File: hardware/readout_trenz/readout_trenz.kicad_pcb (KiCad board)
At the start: 6 copper layers, 377 parts, among them J1 Conn_Coaxial, J10 SparkfunFT232RL, J11 TrenzSFP+cage, J12 Trenz_Module, J13 Conn_02x05_Odd_Even, J14 BNC, J15 ERM8-060-05.0-L-DV, J16 ERM8-060-05.0-L-DV, J17 ERM8-060-05.0-L-DV, J18 ERM8-060-05.0-L-DV, J19 ERM8-060-05.0-L-DV, J2 Conn_Coaxial, J3 Conn_Coaxial_Power, J4 Conn_02x05_Odd_Even, J5 Conn_01x10, J7 BNC, J8 ERM8-060-05.0-L-DV, J9 Digilent JTAG header, Q1 DMN67D7L, Q2 DMN67D7L, Q3 DMN67D7L, Q4 DMN67D7L, Q5 DMN67D7L, Q6 DMN67D7L, U1 SN74AXC2T45DCTR, U10 NLSV8T244, U11 DS90LV027A, U12 ADS7955, U13 REF5025, U14 SN74AXC2T45DCTR, U15 CITIROC1A, U16 SN74AXC2T45DCTR, U17 NLSV8T244, U18 NLSV8T244, U19 DS90LV027A, U2 LP2985-5.0, U20 ADS7955, U21 REF5025, U22 SN74AXC2T45DCTR, U3 NCP718xSN180, U4 LT1963AxQ-3.3, U5 LT1963AxQ-3.3, U6 LT1963AxQ-3.3, U7 CITIROC1A, U8 SN74AXC2T45DCTR, U9 NLSV8T244

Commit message: -
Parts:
- removed the U15 at (348.6, 175.0)
- moved C89 3.39 mm to (397.6, 136.3), turned to 0 degrees
- moved C171 3.39 mm to (339.0, 136.9), turned to 0 degrees
- moved C70 3.39 mm to (412.1, 161.2), turned to 270 degrees
- moved C88 3.39 mm to (397.6, 139.7), turned to 0 degrees
- moved C74 3.38 mm to (415.5, 161.2), turned to 90 degrees
- moved C172 3.38 mm to (339.0, 133.5), turned to 0 degrees
- moved C77 2.61 mm to (416.4, 168.0)
- moved C80 2.26 mm to (418.0, 122.3)
- moved C163 2.26 mm to (317.5, 132.6)
- moved C69 2.23 mm to (408.6, 122.3)
- moved C68 2.17 mm to (408.6, 138.9)
- moved C79 2.15 mm to (417.9, 138.9)
- moved C152 2.10 mm to (326.9, 132.6)
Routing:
- net 3.3V_CITIROC: track 88.0 -> 65.3 mm, vias 40 -> 30
- net GNDD: track 37.0 -> 28.0 mm, vias 37 -> 28
- net GNDA: track 96.0 -> 89.0 mm, vias 55 -> 48
- net 1.8V_CITIROC: track 15.5 -> 10.4 mm, vias 12 -> 8
- net Net-(C154-Pad2): track 9.10 -> 4.55 mm, vias 2 -> 1
- net Net-(C150-Pad2): track 8.25 -> 4.12 mm, vias 4 -> 2
- net Net-(TP16-Pad1): track 7.65 -> 3.82 mm
- net Net-(R111-Pad2): track 6.52 -> 2.84 mm, vias 2 -> 1
- net /CITIROC_1/Fast_Trig1: track 5.87 -> 2.94 mm, vias 2 -> 1
- net Net-(C148-Pad2): track 5.57 -> 2.79 mm, vias 2 -> 1
- net Net-(TP15-Pad1): track 5.41 -> 2.71 mm
- net Net-(C149-Pad2): track 5.41 -> 2.71 mm, vias 2 -> 1
- net Net-(R112-Pad2): track 4.92 -> 2.46 mm, vias 2 -> 1
- net Net-(R112-Pad1): track 4.87 -> 2.46 mm, vias 2 -> 1
- net Net-(R111-Pad1): track 4.96 -> 2.73 mm, vias 2 -> 1
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
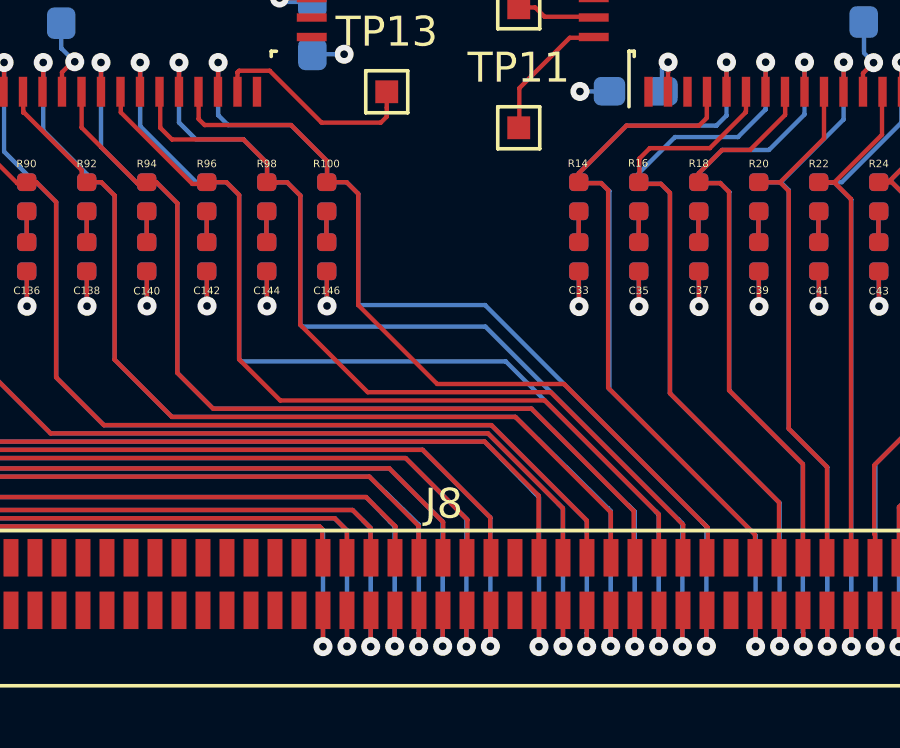
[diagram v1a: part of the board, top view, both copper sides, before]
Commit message: Readout Prototype Layout in progress
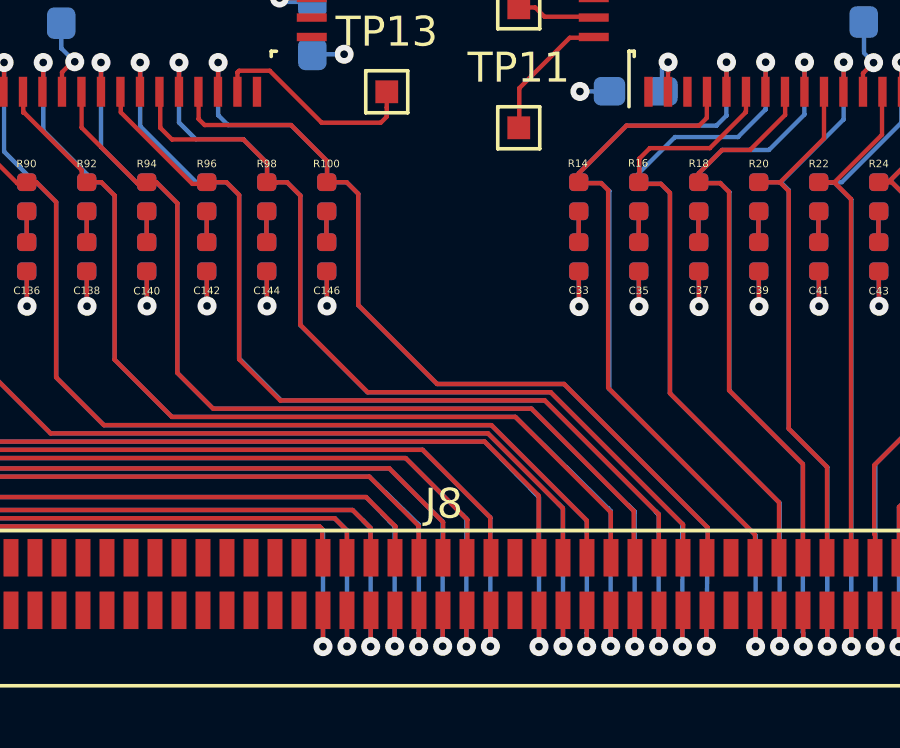
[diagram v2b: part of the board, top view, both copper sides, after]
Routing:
- net /CITIROC_1/SIPM_IN29: track 33.8 -> 34.7 mm

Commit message: Layout in progress
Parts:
- added J6: Conn_01x10, Connector_PinHeader_2.54mm:PinHeader_2x05_P2.54mm_Vertical, F.Cu at (214.2, 144.8)
- C96: moved to B.Cu
- J4: footprint Connector_PinHeader_2.54mm:PinHeader_2x05_P2.54mm_Vertical -> Connector_PinHeader_2.54mm:PinHeader_2x04_P2.54mm_Vertical
- U10, U17, U18, U9: footprint Package_SO:SOIC-20W_7.5x12.8mm_P1.27mm -> Package_SO:TSSOP-20_4.4x6.5mm_P0.65mm
- moved U10 57.5 mm to (356.7, 116.2), turned to 270 degrees
- moved U9 56.4 mm to (363.9, 116.2), turned to 270 degrees
- moved C162 51.1 mm to (366.8, 135.4), turned to 180 degrees
- moved C151 44.6 mm to (366.8, 129.5), turned to 180 degrees
- moved U17 44.4 mm to (365.0, 132.4), turned to 270 degrees
- moved C163 42.2 mm to (359.6, 135.3), turned to 180 degrees
- moved R105 39.5 mm to (310.0, 142.5), turned to 0 degrees
- moved R51 38.6 mm to (426.0, 157.5), turned to 0 degrees
- moved R106 36.4 mm to (310.0, 145.0), turned to 0 degrees
- moved R52 36.0 mm to (426.0, 155.0), turned to 0 degrees
- moved U18 35.9 mm to (357.9, 132.4), turned to 270 degrees
- moved R46 33.6 mm to (426.0, 152.5), turned to 0 degrees
- moved R104 33.4 mm to (310.0, 147.5), turned to 0 degrees
- moved C152 32.9 mm to (359.6, 129.5), turned to 180 degrees
- moved R47 31.4 mm to (426.0, 150.0), turned to 0 degrees
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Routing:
- net /CITIROC_1/TRIG_OUT26: track 0.00 -> 22.9 mm, vias 0 -> 2
- net /CITIROC_1/TRIG_OUT30: track 0.00 -> 21.5 mm, vias 0 -> 2
- net /CITIROC_1/TRIG_OUT28: track 0.00 -> 21.3 mm, vias 0 -> 2
- net /CITIROC_1/TRIG_OUT29: track 0.00 -> 19.8 mm, vias 0 -> 2
- net /CITIROC_1/TRIG_OUT25: track 0.00 -> 19.1 mm, vias 0 -> 2
- net /CITIROC_1/TRIG_OUT27: track 0.00 -> 17.1 mm
- net /CITIROC_1/TRIG_OUT31: track 0.00 -> 16.9 mm
- net GNDA: track 89.0 -> 103.3 mm, vias 48 -> 54
- net GNDD: track 28.0 -> 41.3 mm
- net 3.3V_CITIROC: track 65.3 -> 68.5 mm
- net 1.8V_CITIROC: track 10.4 -> 13.5 mm
- net /CITIROC_1/SIPM_IN30: track 27.0 -> 25.0 mm, vias 0 -> 2
- net /CITIROC_1/SIPM_IN31: track 32.5 -> 30.6 mm, vias 2 -> 3
- net /CITIROC_1/SIPM_IN19: track 38.9 -> 37.1 mm, vias 2 -> 3
- net /CITIROC_1/SIPM_IN3: track 52.2 -> 50.7 mm, vias 2 -> 3
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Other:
- net class Power added: clearance 0.127, trace_width 0.254, via_dia 0.635, via_drill 0.254

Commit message: Layout in progress
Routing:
- net /CITIROC_1/TRIG_OUT5: track 0.00 -> 39.9 mm, vias 0 -> 2
- net /CITIROC_1/TRIG_OUT9: track 0.00 -> 39.9 mm, vias 0 -> 2
- net /CITIROC_1/TRIG_OUT13: track 0.00 -> 39.8 mm, vias 0 -> 2
- net /CITIROC_1/TRIG_OUT12: track 0.00 -> 39.5 mm, vias 0 -> 2
- net /CITIROC_1/TRIG_OUT8: track 0.00 -> 39.5 mm, vias 0 -> 2
- net /CITIROC_1/TRIG_OUT4: track 0.00 -> 39.1 mm, vias 0 -> 2
- net /CITIROC_1/TRIG_OUT1: track 0.00 -> 36.8 mm, vias 0 -> 2
- net /CITIROC_1/TRIG_OUT0: track 0.00 -> 35.7 mm, vias 0 -> 2
- net /CITIROC_1/TRIG_OUT10: track 0.00 -> 33.7 mm, vias 0 -> 2
- net /CITIROC_1/TRIG_OUT11: track 0.00 -> 33.5 mm, vias 0 -> 2
- net /CITIROC_1/TRIG_OUT6: track 0.00 -> 33.4 mm, vias 0 -> 2
- net /CITIROC_1/TRIG_OUT7: track 0.00 -> 33.4 mm, vias 0 -> 2
- net /CITIROC_1/TRIG_OUT2: track 0.00 -> 33.1 mm, vias 0 -> 2
- net /CITIROC_1/TRIG_OUT3: track 0.00 -> 33.0 mm, vias 0 -> 2
- net /CITIROC_1/TRIG_OUT14: track 0.00 -> 32.8 mm, vias 0 -> 2
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
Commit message: Layout in progress
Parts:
- R102, R103, R104, R105, R106, R107, R108, R46, R47, R48, R49, R50, R51, R52, U14, U16, U19, U22: moved to B.Cu
- moved R103 59.4 mm to (359.6, 182.7)
- moved R104 59.1 mm to (359.6, 179.7)
- moved R102 58.9 mm to (359.6, 184.2)
- moved R105 58.5 mm to (359.6, 173.6)
- moved R108 58.3 mm to (359.6, 185.7)
- moved R106 58.0 mm to (359.6, 175.1)
- moved R107 57.8 mm to (359.6, 187.2)
- moved C80 44.1 mm to (374.9, 131.8), turned to 180 degrees
- moved R47 43.0 mm to (398.0, 182.6)
- moved R48 42.6 mm to (398.0, 179.6)
- moved R46 42.2 mm to (398.0, 184.1)
- moved R49 41.8 mm to (398.0, 173.6)
- moved R52 41.5 mm to (398.0, 185.6)
- moved R50 41.1 mm to (398.0, 175.1)
- moved R51 40.7 mm to (398.0, 187.1)
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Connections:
- J12 pad A31: /CITIROC_1/ADC_SERIAL0 -> /CITIROC_2/Serial_ctrl0
- J12 pad A32: /CITIROC_2/ADC_SERIAL0 -> /CITIROC_2/SH_Ctrl0
- J12 pad A33: /CITIROC_1/ADC_SERIAL1 -> /CITIROC_2/Serial_ctrl1
- J12 pad A34: /CITIROC_2/ADC_SERIAL1 -> /CITIROC_2/SH_Ctrl1
- J12 pad A35: /CITIROC_1/ADC_SERIAL2 -> /CITIROC_2/Serial_ctrl2
- J12 pad A36: /CITIROC_2/ADC_SERIAL2 -> /CITIROC_2/SH_Ctrl2
- J12 pad A37: /CITIROC_1/ADC_SERIAL3 -> /CITIROC_2/Serial_ctrl3
- J12 pad A38: /CITIROC_2/ADC_SERIAL3 -> /CITIROC_2/SH_Ctrl3
- J12 pad A39: /CITIROC_1/SH_Ctrl0 -> /CITIROC_2/Serial_ctrl4
- J12 pad A40: /CITIROC_2/SH_Ctrl0 -> /CITIROC_2/SH_Ctrl4
- J12 pad A41: /CITIROC_1/SH_Ctrl1 -> /CITIROC_2/Serial_ctrl5
- J12 pad A42: /CITIROC_2/SH_Ctrl1 -> /CITIROC_2/SH_Ctrl5
- J12 pad A43: /CITIROC_1/SH_Ctrl2 -> /CITIROC_2/Serial_ctrl6
- J12 pad A44: /CITIROC_2/SH_Ctrl2 -> /CITIROC_2/SH_Ctrl6
- J12 pad A45: /CITIROC_1/SH_Ctrl3 -> /CITIROC_2/Serial_ctrl7
- J12 pad A46: /CITIROC_2/SH_Ctrl3 -> /CITIROC_2/SH_Ctrl7
- J12 pad A49: /CITIROC_1/SH_Ctrl4 -> /CITIROC_2/Serial_ctrl8
- J12 pad A50: /CITIROC_2/SH_Ctrl4 -> /CITIROC_2/SH_Ctrl8
- J12 pad A51: /CITIROC_1/SH_Ctrl5 -> /CITIROC_1/SH_Ctrl0
- J12 pad A52: /CITIROC_2/SH_Ctrl5 -> /CITIROC_2/SH_Ctrl9
- J12 pad A53: /CITIROC_1/SH_Ctrl6 -> /CITIROC_1/SH_Ctrl1
- J12 pad A54: /CITIROC_2/SH_Ctrl6 -> /CITIROC_1/ADC_SERIAL0
- J12 pad A55: /CITIROC_1/SH_Ctrl7 -> /CITIROC_1/SH_Ctrl2
- J12 pad A56: /CITIROC_2/SH_Ctrl7 -> /CITIROC_1/ADC_SERIAL1
- J12 pad A57: /CITIROC_1/SH_Ctrl8 -> /CITIROC_1/SH_Ctrl3
- J12 pad A58: /CITIROC_2/SH_Ctrl8 -> /CITIROC_1/ADC_SERIAL2
- J12 pad A59: /CITIROC_1/SH_Ctrl9 -> /CITIROC_1/SH_Ctrl4
- J12 pad A60: /CITIROC_2/SH_Ctrl9 -> /CITIROC_1/ADC_SERIAL3
- J12 pad A62: /Trenz_Module/TEST0 -> /CITIROC_2/ADC_SERIAL0
- J12 pad A63: /Trenz_Module/TEST1 -> /CITIROC_1/SH_Ctrl5
- J12 pad A64: /CITIROC_2/Serial_ctrl0 -> /CITIROC_2/ADC_SERIAL1
- J12 pad A65: /CITIROC_1/Serial_ctrl0 -> /CITIROC_1/SH_Ctrl6
- J12 pad A67: /CITIROC_1/Serial_ctrl1 -> /CITIROC_1/SH_Ctrl7
- J12 pad A68: /CITIROC_2/Serial_ctrl1 -> /CITIROC_2/ADC_SERIAL2
- J12 pad A69: /CITIROC_1/Serial_ctrl2 -> /CITIROC_1/SH_Ctrl8
- J12 pad A70: /CITIROC_2/Serial_ctrl2 -> /CITIROC_2/ADC_SERIAL3
- J12 pad A71: /CITIROC_1/Serial_ctrl3 -> /CITIROC_1/SH_Ctrl9
- J12 pad A72: /CITIROC_2/Serial_ctrl3 -> /CITIROC_1/Fast_Trig0
- J12 pad A73: /CITIROC_1/Serial_ctrl4 -> /CITIROC_1/Serial_ctrl0
- J12 pad A74: /CITIROC_2/Serial_ctrl4 -> /CITIROC_1/Fast_Trig1
- J12 pad A75: /CITIROC_1/Serial_ctrl5 -> /CITIROC_1/Serial_ctrl1
- J12 pad A76: /CITIROC_2/Serial_ctrl5 -> /CITIROC_1/Fast_Trig2
- J12 pad A77: /CITIROC_1/Serial_ctrl6 -> /CITIROC_1/Serial_ctrl2
- J12 pad A78: /CITIROC_2/Serial_ctrl6 -> /CITIROC_1/Fast_Trig3
- J12 pad A79: /CITIROC_1/Serial_ctrl7 -> /CITIROC_1/Serial_ctrl3
- J12 pad A80: /CITIROC_2/Serial_ctrl7 -> /Trenz_Module/TEST0
- J12 pad A81: /CITIROC_1/Serial_ctrl8 -> /CITIROC_1/Serial_ctrl4
- J12 pad A82: /CITIROC_2/Serial_ctrl8 -> /Trenz_Module/TEST1
- J12 pad A85: /POWER/ENABLE -> /CITIROC_1/Serial_ctrl5
- J12 pad A87: /Trenz_Module/TEST2 -> /CITIROC_1/Serial_ctrl6
- J12 pad A89: /CITIROC_1/Fast_Trig0 -> /CITIROC_1/Serial_ctrl7
- J12 pad A91: /CITIROC_1/Fast_Trig1 -> /CITIROC_1/Serial_ctrl8
- J12 pad A93: /CITIROC_1/Fast_Trig2 -> /Trenz_Module/TEST2
- J12 pad A95: /CITIROC_1/Fast_Trig3 -> /POWER/ENABLE
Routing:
- net /CITIROC_2/Serial_ctrl3: track 0.00 -> 10.2 mm
- net /CITIROC_2/Serial_ctrl2: track 0.00 -> 10.1 mm
- net /CITIROC_2/Serial_ctrl0: track 0.00 -> 10.1 mm
- net /CITIROC_2/Serial_ctrl1: track 0.00 -> 10.0 mm
- net /CITIROC_2/Serial_ctrl4: track 0.00 -> 9.79 mm
- net /CITIROC_2/Serial_ctrl5: track 0.00 -> 9.47 mm
- net /CITIROC_2/Serial_ctrl6: track 0.00 -> 9.14 mm
- net /CITIROC_1/Serial_ctrl4: track 0.00 -> 7.97 mm
- net /CITIROC_1/Serial_ctrl3: track 0.00 -> 7.94 mm
- net /CITIROC_1/Serial_ctrl6: track 0.00 -> 7.89 mm
- net /CITIROC_1/Serial_ctrl2: track 0.00 -> 7.87 mm
- net /CITIROC_1/Serial_ctrl1: track 0.00 -> 7.76 mm
- net /CITIROC_1/Serial_ctrl5: track 0.00 -> 7.75 mm
- net /CITIROC_1/Serial_ctrl0: track 0.00 -> 7.72 mm
- net /CITIROC_1/SH_Ctrl5: track 0.00 -> 6.99 mm
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
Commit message: Layout ion progress
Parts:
- added C12: 1uF, Capacitor_SMD:C_0603_1608Metric_Pad1.05x0.95mm_HandSolder, F.Cu at (253.3, 132.2)
- added C7: 1uF, Capacitor_SMD:C_0603_1608Metric_Pad1.05x0.95mm_HandSolder, F.Cu at (244.8, 131.3)
- added D9: Red_LED, LED_THT:LED_D3.0mm, F.Cu at (230.0, 102.4)
- added Q3: DMN67D7L, Package_TO_SOT_SMD:SOT-23, F.Cu at (232.2, 107.2)
- added R14: 80, Resistor_SMD:R_0603_1608Metric_Pad1.05x0.95mm_HandSolder, F.Cu at (229.6, 106.3)
- added U4: NCP718xSN180, Package_TO_SOT_SMD:TSOT-23-5_HandSoldering, F.Cu at (249.5, 132.3)
- C162: renamed from C160; moved to F.Cu
- C79: renamed from C77; moved to F.Cu
- U12: renamed from U11; moved to B.Cu
- U9: renamed from U8; moved to B.Cu
- moved U17 52.1 mm to (363.0, 135.0)
- moved U20 50.8 mm to (367.8, 159.8), turned to 270 degrees
- moved C162 50.5 mm to (366.8, 157.3), turned to 180 degrees
- moved C159 50.2 mm to (359.5, 136.3), turned to 0 degrees
- moved C155 48.5 mm to (359.5, 133.7), turned to 180 degrees
- moved C76 43.8 mm to (379.5, 136.3), turned to 0 degrees
- moved C72 42.6 mm to (379.5, 133.7), turned to 180 degrees
- moved U9 40.4 mm to (383.0, 135.0), turned to 270 degrees
- moved C88 39.9 mm to (374.5, 69.2)
- moved U21 39.9 mm to (365.3, 69.0)
- moved C157 39.9 mm to (350.5, 79.8)
- moved C158 39.9 mm to (348.0, 79.8)
- moved C160 39.9 mm to (345.5, 79.8)
- moved C161 39.9 mm to (358.0, 79.8)
- moved C163 39.9 mm to (360.5, 79.8)
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- renumbered C9 to C10, C98 to C100, C99 to C101, C100 to C102, C101 to C103, C102 to C104, C103 to C105, C104 to C106, C105 to C107, C106 to C108, C107 to C109, C10 to C11, C108 to C110, C109 to C111, C110 to C112, C111 to C113, C112 to C114, C113 to C115, C114 to C116, C115 to C117, C116 to C118, C117 to C119, C118 to C120, C119 to C121, C120 to C122, C121 to C123, C122 to C124, C123 to C125, C124 to C126, C125 to C127, C126 to C128, C127 to C129, C11 to C13, C128 to C130, C129 to C131, C130 to C132, C131 to C133, C132 to C134, C133 to C135, C134 to C136, C135 to C137, C136 to C138, C137 to C139, C12 to C14, C138 to C140, C139 to C141, C140 to C142, C141 to C143, C142 to C144, C143 to C145, C144 to C146, C145 to C147, C146 to C148, C147 to C149, C13 to C15, C148 to C150, C149 to C151, C150 to C152, C151 to C153, C152 to C154, C153 to C155, C154 to C156, C155 to C157, C156 to C158, C157 to C159, C14 to C16, C158 to C160, C159 to C161, C161 to C163, C162 to C164, C163 to C165, C164 to C166, C165 to C167, C166 to C168, C167 to C169, C15 to C17, C168 to C170, C169 to C171, C170 to C172, C171 to C173, C172 to C174, C16 to C18, C17 to C19, C18 to C20, C19 to C21, C20 to C22, C21 to C23, C22 to C24, C23 to C25, C24 to C26, C25 to C27, C26 to C28, C27 to C29, C28 to C30, C29 to C31, C30 to C32, C31 to C33, C32 to C34, C33 to C35, C34 to C36, C35 to C37, C36 to C38, C37 to C39, C38 to C40, C39 to C41, C40 to C42, C41 to C43, C42 to C44, C43 to C45, C44 to C46, C45 to C47, C46 to C48, C47 to C49, C48 to C50, C49 to C51, C50 to C52, C51 to C53, C52 to C54, C53 to C55, C54 to C56, C55 to C57, C56 to C58, C57 to C59, C58 to C60, C59 to C61, C60 to C62, C61 to C63, C62 to C64, C63 to C65, C64 to C66, C65 to C67, C66 to C68, C67 to C69, C68 to C70, C69 to C71, C70 to C72, C71 to C73, C72 to C74, C73 to C75, C74 to C76, C75 to C77, C76 to C78, C7 to C8, C78 to C80, C79 to C81, C80 to C82, C81 to C83, C82 to C84, C83 to C85, C84 to C86, C85 to C87, C86 to C88, C87 to C89, C8 to C9, C88 to C90, C89 to C91, C90 to C92, C91 to C93, C92 to C94, C93 to C95, C94 to C96, C95 to C97, C96 to C98, C97 to C99, D9 to D10, D10 to D11, D11 to D12, D12 to D13, J17 to J10, J8 to J11, J18 to J12, J19 to J13, J9 to J14, J10 to J15, J11 to J16, J12 to J17, J13 to J18, J14 to J19, J15 to J8, J16 to J9, Q3 to Q4, Q4 to Q5, Q5 to Q6, Q6 to Q7, R99 to R100, R100 to R101, R101 to R102, R102 to R103, R103 to R104, R104 to R105, R105 to R106, R106 to R107, R107 to R108, R108 to R109, R109 to R110, R110 to R111, R111 to R112, R112 to R113, R113 to R114, R114 to R115, R115 to R116, R116 to R117, R14 to R15, R15 to R16, R16 to R17, R17 to R18, R18 to R19, R19 to R20, R20 to R21, R21 to R22, R22 to R23, R23 to R24, R24 to R25, R25 to R26, R26 to R27, R27 to R28, R28 to R29, R29 to R30, R30 to R31, R31 to R32, R32 to R33, R33 to R34, R34 to R35, R35 to R36, R36 to R37, R37 to R38, R38 to R39, R39 to R40, R40 to R41, R41 to R42, R42 to R43, R43 to R44, R44 to R45, R45 to R46, R46 to R47, R47 to R48, R48 to R49, R49 to R50, R50 to R51, R51 to R52, R52 to R53, R53 to R54, R54 to R55, R55 to R56, R56 to R57, R57 to R58, R58 to R59, R59 to R60, R60 to R61, R61 to R62, R62 to R63, R63 to R64, R64 to R65, R65 to R66, R66 to R67, R67 to R68, R68 to R69, R69 to R70, R70 to R71, R71 to R72, R72 to R73, R73 to R74, R74 to R75, R75 to R76, R76 to R77, R77 to R78, R78 to R79, R79 to R80, R80 to R81, R81 to R82, R82 to R83, R83 to R84, R84 to R85, R85 to R86, R86 to R87, R87 to R88, R88 to R89, R89 to R90, R90 to R91, R91 to R92, R92 to R93, R93 to R94, R94 to R95, R95 to R96, R96 to R97, R97 to R98, R98 to R99, U9 to U10, U10 to U11, U12 to U13, U13 to U14, U14 to U15, U15 to U16, U16 to U17, U17 to U18, U18 to U19, U19 to U20, U20 to U21, U21 to U22, U22 to U23, U4 to U5, U5 to U6, U6 to U7, U7 to U8
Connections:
- C1 pad 2: GNDD -> GND
- C10 pad 2: GNDD -> GND
- C100 pad 2: GNDA -> GND
- C101 pad 2: GNDD -> GND
- C102 pad 1: GNDA -> GND
- C103 pad 1: GNDA -> GND
- C104 pad 2: GNDD -> GND
- C105 pad 2: GNDD -> GND
- C106 pad 2: GNDD -> GND
- C107 pad 2: GNDD -> GND
- C108 pad 2: GNDD -> GND
- C109 pad 2: GNDD -> GND
- C11 pad 2: GNDD -> GND
- C110 pad 2: GNDD -> GND
- C111 pad 2: GNDD -> GND
- C112 pad 2: GNDD -> GND
- C113 pad 2: GNDD -> GND
- C114 pad 2: GNDD -> GND
- C115 pad 2: GNDD -> GND
- C116 pad 2: GNDD -> GND
- C117 pad 2: GNDD -> GND
- C118 pad 2: GNDA -> GND
- C119 pad 2: GNDA -> GND
- C120 pad 2: GNDA -> GND
- C121 pad 2: GNDA -> GND
- C122 pad 2: GNDA -> GND
- C123 pad 2: GNDA -> GND
- C124 pad 2: GNDA -> GND
- C125 pad 2: GNDA -> GND
- C126 pad 2: GNDA -> GND
- C127 pad 2: GNDA -> GND
- C128 pad 2: GNDA -> GND
- C129 pad 2: GNDA -> GND
- C13 pad 2: GNDD -> GND
- C130 pad 2: GNDA -> GND
- C131 pad 2: GNDA -> GND
- C132 pad 2: GNDA -> GND
- C133 pad 2: GNDA -> GND
- C134 pad 2: GNDA -> GND
- C135 pad 2: GNDA -> GND
- C136 pad 2: GNDA -> GND
- C137 pad 2: GNDA -> GND
- C138 pad 2: GNDA -> GND
- C139 pad 2: GNDA -> GND
- C14 pad 2: GNDD -> GND
- C140 pad 2: GNDA -> GND
- C141 pad 2: GNDA -> GND
- C142 pad 2: GNDA -> GND
- C143 pad 2: GNDA -> GND
- C144 pad 2: GNDA -> GND
- C145 pad 2: GNDA -> GND
- C146 pad 2: GNDA -> GND
- C147 pad 2: GNDA -> GND
- C148 pad 2: GNDA -> GND
- C149 pad 2: GNDA -> GND
- C15 pad 2: GNDD -> GND
- C150 pad 1: GNDA -> GND
- C151 pad 1: GNDA -> GND
- C152 pad 1: GNDA -> GND
- C153 pad 2: GNDD -> GND
- C154 pad 2: GNDD -> GND
- C155 pad 2: GNDD -> GND
- C156 pad 1: GNDA -> GND
- C157 pad 2: GNDA -> GND
- C158 pad 2: GNDA -> GND
- C159 pad 1: GNDD -> GND
- C16 pad 2: GNDA -> GND
- C160 pad 2: GNDA -> GND
- C161 pad 2: GNDA -> GND
- C162 pad 1: GNDD -> GND
- C163 pad 2: GNDA -> GND
- C164 pad 2: GNDD -> GND
- C165 pad 2: GNDD -> GND
- C166 pad 2: GNDA -> GND
- C167 pad 2: GNDA -> GND
- C168 pad 1: GNDD -> GND
- C169 pad 2: GNDD -> GND
- C17 pad 2: GNDA -> GND
- C170 pad 2: GNDA -> GND
- C171 pad 2: GNDA -> GND
- C172 pad 2: GNDD -> GND
- C173 pad 1: GNDD -> GND
- C174 pad 1: GNDD -> GND
- C18 pad 2: GNDD -> GND
- C19 pad 1: GNDA -> GND
- C2 pad 1: GNDD -> GND
- C20 pad 1: GNDA -> GND
- C21 pad 2: GNDD -> GND
- C22 pad 2: GNDD -> GND
- C23 pad 2: GNDD -> GND
- C24 pad 2: GNDD -> GND
- C25 pad 2: GNDD -> GND
- C26 pad 2: GNDD -> GND
- C27 pad 2: GNDD -> GND
- C28 pad 2: GNDD -> GND
- C29 pad 2: GNDD -> GND
- C3 pad 2: GNDD -> GND
- C30 pad 2: GNDD -> GND
- C31 pad 2: GNDD -> GND
- C32 pad 2: GNDD -> GND
- C33 pad 2: GNDD -> GND
- C34 pad 2: GNDD -> GND
- C35 pad 2: GNDA -> GND
- C36 pad 2: GNDA -> GND
- C37 pad 2: GNDA -> GND
- C38 pad 2: GNDA -> GND
- C39 pad 2: GNDA -> GND
- C4 pad 2: GNDD -> GND
- C40 pad 2: GNDA -> GND
- C41 pad 2: GNDA -> GND
- C42 pad 2: GNDA -> GND
- C43 pad 2: GNDA -> GND
- C44 pad 2: GNDA -> GND
- C45 pad 2: GNDA -> GND
- C46 pad 2: GNDA -> GND
- C47 pad 2: GNDA -> GND
- C48 pad 2: GNDA -> GND
- C49 pad 2: GNDA -> GND
- C5 pad 2: GNDD -> GND
- C50 pad 2: GNDA -> GND
- C51 pad 2: GNDA -> GND
- C52 pad 2: GNDA -> GND
- C53 pad 2: GNDA -> GND
- C54 pad 2: GNDA -> GND
- C55 pad 2: GNDA -> GND
- C56 pad 2: GNDA -> GND
- C57 pad 2: GNDA -> GND
- C58 pad 2: GNDA -> GND
- C59 pad 2: GNDA -> GND
- C6 pad 2: GNDD -> GND
- C60 pad 2: GNDA -> GND
- C61 pad 2: GNDA -> GND
- C62 pad 2: GNDA -> GND
- C63 pad 2: GNDA -> GND
- C64 pad 2: GNDA -> GND
- C65 pad 2: GNDA -> GND
- C66 pad 2: GNDA -> GND
- C67 pad 1: GNDA -> GND
- C68 pad 1: GNDA -> GND
- C69 pad 1: GNDA -> GND
- C70 pad 2: GNDD -> GND
- C71 pad 2: GNDD -> GND
- C72 pad 2: GNDD -> GND
- C73 pad 1: GNDA -> GND
- C74 pad 2: GNDA -> GND
- C75 pad 2: GNDA -> GND
- C76 pad 1: GNDD -> GND
- C77 pad 2: GNDA -> GND
- C78 pad 2: GNDA -> GND
- C79 pad 1: GNDD -> GND
- C8 pad 2: GNDD -> GND
- C80 pad 2: GNDA -> GND
- C81 pad 2: GNDD -> GND
- C82 pad 2: GNDD -> GND
- C83 pad 2: GNDA -> GND
- C84 pad 2: GNDA -> GND
- C85 pad 1: GNDD -> GND
- C86 pad 2: GNDD -> GND
- C87 pad 2: GNDA -> GND
- C88 pad 2: GNDA -> GND
- C89 pad 2: GNDD -> GND
- C9 pad 2: GNDD -> GND
- C90 pad 1: GNDD -> GND
- C91 pad 1: GNDD -> GND
- C92 pad 2: GNDD -> GND
- C93 pad 2: GNDD -> GND
- C96 pad 2: GNDD -> GND
- C97 pad 2: GNDD -> GND
- C98 pad 2: GNDD -> GND
- C99 pad 2: GNDA -> GND
- D1 pad 1: GNDD -> GND
- D2 pad 1: GNDD -> GND
- D3 pad 1: GNDD -> GND
- D5 pad 1: GNDD -> GND
- D6 pad 1: GNDD -> GND
- D7 pad 1: GNDD -> GND
- J1 pad 2: GNDD -> GND
- J11 pad 1: GNDA -> GND
- J11 pad 19: GNDA -> GND
- J11 pad 2: GNDA -> GND
- J11 pad 20: GNDA -> GND
- J11 pad 37: GNDA -> GND
- J11 pad 38: GNDA -> GND
- J11 pad 55: GNDA -> GND
- J11 pad 56: GNDA -> GND
- J11 pad 73: GNDA -> GND
- J11 pad 74: GNDA -> GND
- J14 pad 1: GNDD -> GND
- J14 pad 11: GNDD -> GND
- J14 pad 13: GNDD -> GND
- J14 pad 3: GNDD -> GND
- J14 pad 5: GNDD -> GND
- J14 pad 7: GNDD -> GND
- J14 pad 9: GNDD -> GND
- J15 pad 4: GNDD -> GND
- J16 pad 1: GNDD -> GND
- J16 pad 10: GNDD -> GND
- J16 pad 11: GNDD -> GND
- J16 pad 14: GNDD -> GND
- J16 pad 17: GNDD -> GND
- J16 pad 20: GNDD -> GND
- J16 pad CAGE: GNDD -> GND
- J17 pad A100: GNDD -> GND
- J17 pad A11: GNDD -> GND
- J17 pad A12: GNDD -> GND
- J17 pad A17: GNDD -> GND
- J17 pad A18: GNDD -> GND
- J17 pad A23: GNDD -> GND
- J17 pad A24: GNDD -> GND
- J17 pad A29: GNDD -> GND
- J17 pad A30: GNDD -> GND
- J17 pad A32: /CITIROC_2/SH_Ctrl0 -> /CITIROC_2/SH_Ctrl9
- J17 pad A34: /CITIROC_2/SH_Ctrl1 -> /CITIROC_2/SH_Ctrl8
- J17 pad A36: /CITIROC_2/SH_Ctrl2 -> /CITIROC_2/SH_Ctrl7
- J17 pad A38: /CITIROC_2/SH_Ctrl3 -> /CITIROC_2/SH_Ctrl6
- J17 pad A40: /CITIROC_2/SH_Ctrl4 -> /CITIROC_2/SH_Ctrl5
- J17 pad A42: /CITIROC_2/SH_Ctrl5 -> /CITIROC_2/SH_Ctrl4
- J17 pad A44: /CITIROC_2/SH_Ctrl6 -> /CITIROC_2/SH_Ctrl3
- J17 pad A46: /CITIROC_2/SH_Ctrl7 -> /CITIROC_2/SH_Ctrl2
- J17 pad A47: GNDD -> GND
- J17 pad A48: GNDD -> GND
- J17 pad A5: GNDD -> GND
- J17 pad A50: /CITIROC_2/SH_Ctrl8 -> /CITIROC_2/SH_Ctrl1
- J17 pad A52: /CITIROC_2/SH_Ctrl9 -> /CITIROC_2/SH_Ctrl0
- J17 pad A6: GNDD -> GND
- J17 pad A66: GNDD -> GND
- J17 pad A72: /CITIROC_1/Fast_Trig0 -> /CITIROC_1/Fast_Trig3
- J17 pad A74: /CITIROC_1/Fast_Trig1 -> /CITIROC_1/Fast_Trig2
- J17 pad A76: /CITIROC_1/Fast_Trig2 -> /CITIROC_1/Fast_Trig1
- J17 pad A78: /CITIROC_1/Fast_Trig3 -> /CITIROC_1/Fast_Trig0
- J17 pad A84: GNDD -> GND
- J17 pad A98: GNDD -> GND
- J17 pad B17: GNDD -> GND
- J17 pad B35: GNDD -> GND
- J17 pad B36: GNDD -> GND
- J17 pad B72: GNDD -> GND
- J17 pad B83: GNDD -> GND
- J17 pad B90: GNDD -> GND
- J18 pad 10: GNDD -> GND
- J18 pad 2: GNDD -> GND
- J18 pad 4: GNDD -> GND
- J18 pad 6: GNDD -> GND
- J18 pad 8: GNDD -> GND
- J19 pad 2: GNDA -> GND
- J2 pad 2: GNDD -> GND
- J3 pad 2: GNDD -> GND
- J4 pad 2: GNDA -> GND
- J4 pad 4: GNDA -> GND
- J4 pad 6: GNDA -> GND
- J4 pad 8: GNDA -> GND
- J5 pad 10: GNDD -> GND
- J5 pad 7: GNDD -> GND
- J5 pad 8: GNDD -> GND
- J5 pad 9: GNDD -> GND
- J6 pad 10: GNDD -> GND
- J6 pad 7: GNDD -> GND
- J6 pad 8: GNDD -> GND
- J6 pad 9: GNDD -> GND
- J7 pad 2: GNDA -> GND
- Q1 pad 2: GNDD -> GND
- Q2 pad 2: GNDD -> GND
- Q4 pad 2: GNDD -> GND
- Q5 pad 2: GNDD -> GND
- Q6 pad 2: GNDD -> GND
- Q7 pad 2: GNDD -> GND
- R1 pad 2: GNDD -> GND
- R111 pad 2: GNDA -> GND
- R114 pad 2: GNDA -> GND
- R2 pad 2: GNDD -> GND
- R55 pad 2: GNDA -> GND
- R58 pad 2: GNDA -> GND
- R63 pad 2: GNDD -> GND
- R64 pad 2: GNDD -> GND
- R9 pad 1: GNDD -> GND
- TP12 pad 2: GNDD -> GND
- TP24 pad 2: GNDD -> GND
- U1 pad 4: GNDD -> GND
- U1 pad 5: GNDD -> GND
- U10 pad 10: GNDD -> GND
- U10 pad 11: GNDD -> GND
- U11 pad 10: GNDD -> GND
- U11 pad 11: GNDD -> GND
- U12 pad 4: GNDD -> GND
- U13 pad 10: GNDA -> GND
- U13 pad 22: GNDA -> GND
- U13 pad 27: GNDD -> GND
- U13 pad 3: GNDA -> GND
- U13 pad 6: GNDA -> GND
- U13 pad 9: GNDA -> GND
- U14 pad 4: GNDA -> GND
- U15 pad 4: GNDD -> GND
- U15 pad 5: GNDD -> GND
- U16 pad 1: GNDA -> GND
- U16 pad 100: GNDD -> GND
- U16 pad 101: GNDD -> GND
- U16 pad 121: GNDD -> GND
- U16 pad 122: GNDD -> GND
- U16 pad 129: GNDD -> GND
- U16 pad 130: GNDA -> GND
- U16 pad 138: GNDA -> GND
- U16 pad 139: GNDA -> GND
- U16 pad 140: GNDA -> GND
- U16 pad 143: GNDD -> GND
- U16 pad 145: GNDA -> GND
- U16 pad 150: GNDA -> GND
- U16 pad 151: GNDA -> GND
- U16 pad 154: GNDA -> GND
- U16 pad 156: GNDA -> GND
- U16 pad 21: GNDA -> GND
- U16 pad 41: GNDA -> GND
- U16 pad 44: GNDA -> GND
- U16 pad 47: GNDA -> GND
- U16 pad 56: GNDA -> GND
- U16 pad 57: GNDA -> GND
- U16 pad 58: GNDA -> GND
- U16 pad 59: GNDA -> GND
- U16 pad 60: GNDA -> GND
- U16 pad 65: GNDA -> GND
- U16 pad 66: GNDD -> GND
- U16 pad 67: GNDD -> GND
- U16 pad 81: GNDD -> GND
- U17 pad 4: GNDD -> GND
- U17 pad 5: GNDD -> GND
- U18 pad 10: GNDD -> GND
- U18 pad 11: GNDD -> GND
- U19 pad 10: GNDD -> GND
- U19 pad 11: GNDD -> GND
- U2 pad 2: GNDD -> GND
- U20 pad 4: GNDD -> GND
- U21 pad 10: GNDA -> GND
- U21 pad 22: GNDA -> GND
- U21 pad 27: GNDD -> GND
- U21 pad 3: GNDA -> GND
- U21 pad 6: GNDA -> GND
- U21 pad 9: GNDA -> GND
- U22 pad 4: GNDA -> GND
- U23 pad 4: GNDD -> GND
- U23 pad 5: GNDD -> GND
- U3 pad 2: GNDD -> GND
- U5 pad 3: GNDD -> GND
- U6 pad 3: GNDD -> GND
- U7 pad 3: GNDD -> GND
- U8 pad 1: GNDA -> GND
- U8 pad 100: GNDD -> GND
- U8 pad 101: GNDD -> GND
- U8 pad 121: GNDD -> GND
- U8 pad 122: GNDD -> GND
- U8 pad 129: GNDD -> GND
- U8 pad 130: GNDA -> GND
- U8 pad 138: GNDA -> GND
- U8 pad 139: GNDA -> GND
- U8 pad 140: GNDA -> GND
- U8 pad 143: GNDD -> GND
- U8 pad 145: GNDA -> GND
- U8 pad 150: GNDA -> GND
- U8 pad 151: GNDA -> GND
- U8 pad 154: GNDA -> GND
- U8 pad 156: GNDA -> GND
- U8 pad 21: GNDA -> GND
- U8 pad 41: GNDA -> GND
- U8 pad 44: GNDA -> GND
- U8 pad 47: GNDA -> GND
- U8 pad 56: GNDA -> GND
- U8 pad 57: GNDA -> GND
- U8 pad 58: GNDA -> GND
- U8 pad 59: GNDA -> GND
- U8 pad 60: GNDA -> GND
- U8 pad 65: GNDA -> GND
- U8 pad 66: GNDD -> GND
- U8 pad 67: GNDD -> GND
- U8 pad 81: GNDD -> GND
- U9 pad 4: GNDD -> GND
- U9 pad 5: GNDD -> GND
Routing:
- net GND: track 0.00 -> 155.6 mm, vias 0 -> 87
- net GNDA: track 112.6 -> 0.00 mm, vias 58 -> 0
- net /CITIROC_1/Fast_Trig2: track 0.00 -> 50.8 mm, vias 0 -> 2
- net Net-(U16-Pad131): track 0.00 -> 49.3 mm, vias 0 -> 2
- net /CITIROC_1/Fast_Trig3: track 0.00 -> 47.7 mm, vias 0 -> 2
- net Net-(U16-Pad124): track 0.00 -> 46.9 mm, vias 0 -> 2
- net Net-(U16-Pad135): track 0.00 -> 46.4 mm, vias 0 -> 2
- net /CITIROC_1/Fast_Trig1: track 2.94 -> 48.6 mm, vias 1 -> 2
- net Net-(U16-Pad133): track 0.00 -> 45.4 mm, vias 0 -> 1
- net Net-(U16-Pad136): track 0.00 -> 45.3 mm, vias 0 -> 2
- net Net-(U16-Pad134): track 0.00 -> 44.3 mm, vias 0 -> 2
- net Net-(U16-Pad132): track 0.00 -> 41.4 mm, vias 0 -> 2
- net /CITIROC_1/Fast_Trig0: track 2.15 -> 43.2 mm, vias 1 -> 2
- net GNDD: track 40.9 -> 0.00 mm, vias 28 -> 0
- net Net-(U16-Pad126): track 0.00 -> 39.9 mm, vias 0 -> 2
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
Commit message: {
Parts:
- moved C82 7.85 mm to (378.0, 138.9), turned to 270 degrees
- moved C71 7.70 mm to (377.9, 131.2), turned to 90 degrees
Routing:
- net Net-(U16-Pad70): track 0.00 -> 38.6 mm, vias 0 -> 2
- net Net-(U16-Pad71): track 0.00 -> 37.7 mm, vias 0 -> 2
- net Net-(U16-Pad72): track 0.00 -> 35.6 mm, vias 0 -> 2
- net Net-(U11-Pad13): track 0.00 -> 31.4 mm, vias 0 -> 2
- net Net-(U11-Pad14): track 0.00 -> 30.0 mm, vias 0 -> 2
- net Net-(U11-Pad15): track 0.00 -> 28.9 mm, vias 0 -> 2
- net Net-(U16-Pad79): track 0.00 -> 27.0 mm, vias 0 -> 2
- net Net-(R57-Pad2): track 3.05 -> 11.6 mm, vias 1 -> 2
- net Net-(R57-Pad1): track 3.01 -> 11.0 mm, vias 1 -> 2
- net Net-(R56-Pad1): track 2.73 -> 9.03 mm
- net Net-(R56-Pad2): track 2.84 -> 6.48 mm
- net /CITIROC_1/Fast_Trig1: track 48.6 -> 49.3 mm
